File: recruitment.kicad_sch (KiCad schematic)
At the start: 14 parts, among them SW1 SW_SPST

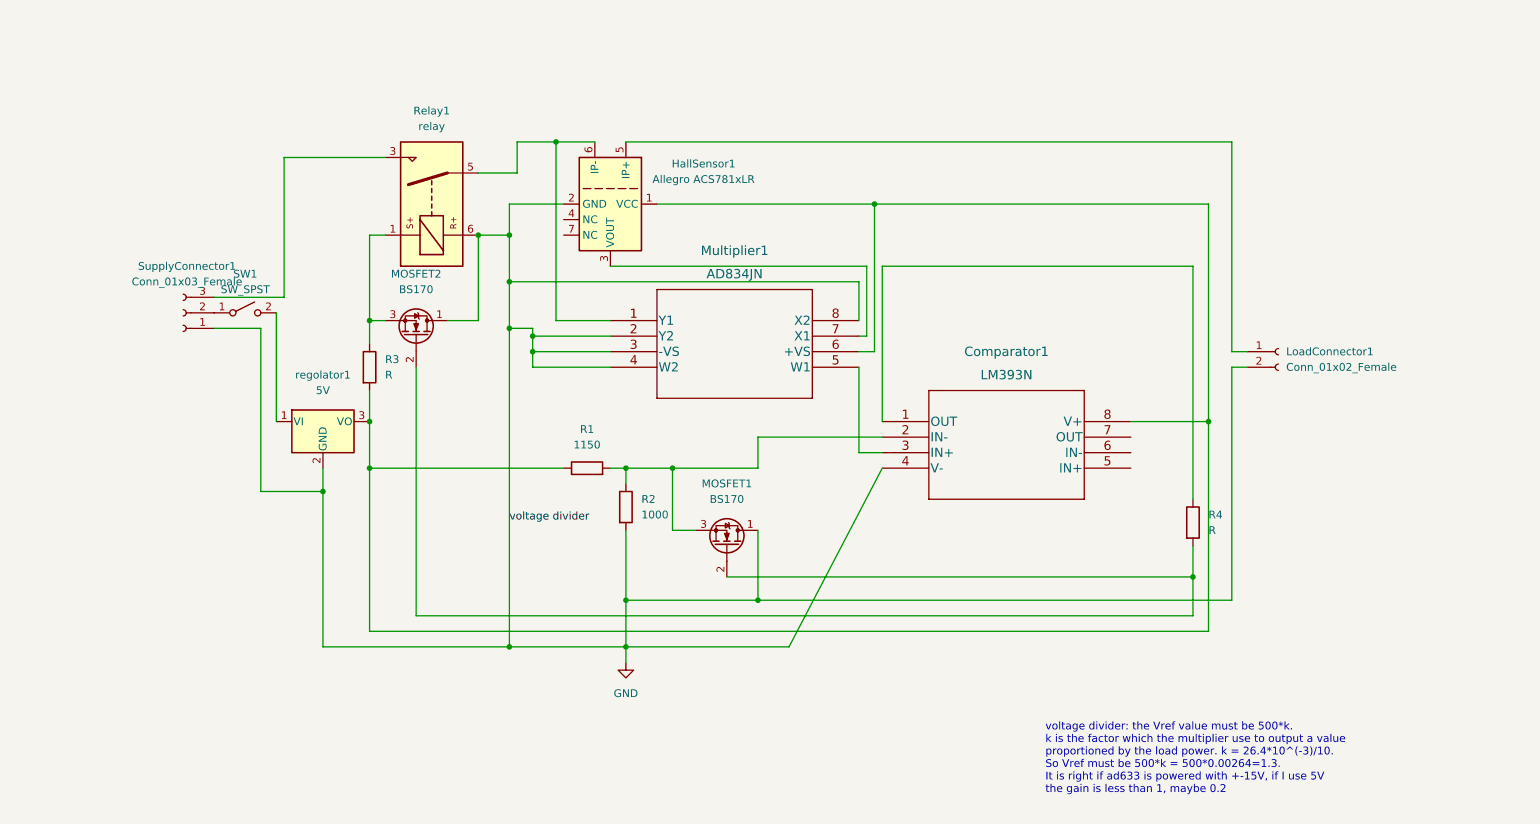
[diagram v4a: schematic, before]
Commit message: TODO: mosfet depletion channel p
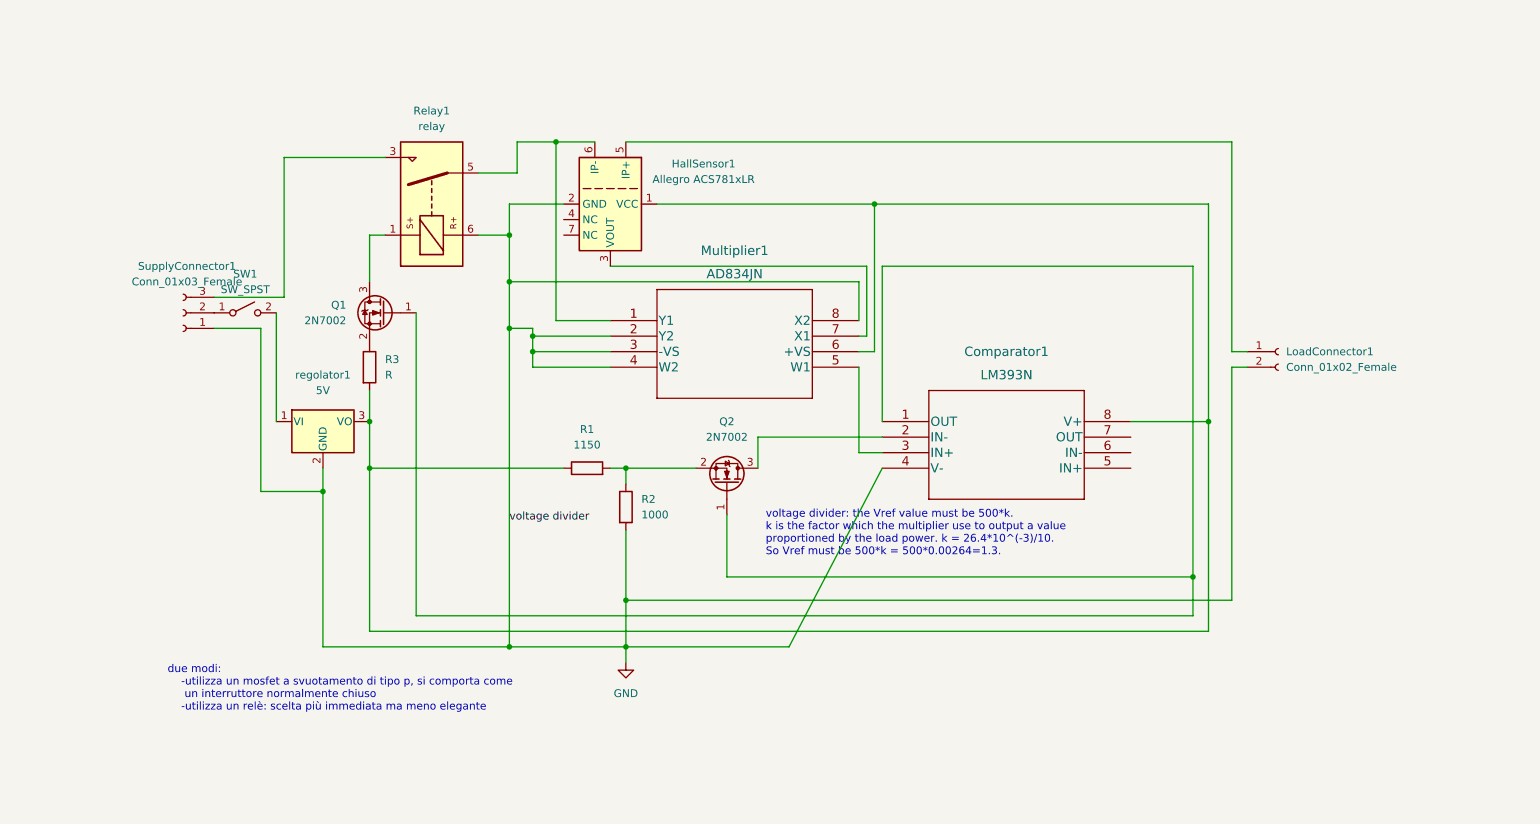
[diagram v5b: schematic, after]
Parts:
- removed MOSFET1, MOSFET2: BS170, Package_TO_SOT_THT:TO-92_Inline, symbol Transistor_FET:BS170
- removed R4: R, Resistor_SMD:R_2816_7142Metric, symbol Device:R
- added Q1, Q2: 2N7002, Package_TO_SOT_SMD:SOT-23, symbol Transistor_FET:2N7002
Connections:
- net at R1.2, R2.1: now also Q2.2 (S); no longer Comparator1.2 (IN-)
- net at R3.1: now also Q1.2 (S); no longer Relay1.1
- net at Comparator1.1 (OUT): now also Q1.1 (G), Q2.1 (G)
- new net: Comparator1.2 (IN-), Q2.3 (D)
- new net: Q1.3 (D), Relay1.1
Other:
- note added: "due modi: -utilizza un mosfet a svuotamento di tipo p, si comporta come un interruttore normalmente chiuso -utilizza un relè: scelta più immediata ma meno elegante"
- note added: "voltage divider: the Vref value must be 500*k. k is the factor which the multiplier use to output a value proportioned by the load power. k = 26.4*10^(-3)/10. So Vref must be 500*k = 500*0.00264=1.3."
- note removed: "voltage divider: the Vref value must be 500*k. k is the factor which the multiplier use to output a value proportioned by the load power. k = 26.4*10^(-3)/10. So Vref must be 500*k = 500*0.00264=1.3. It is right if ad633 is powered with +-15V, if I use 5V the gain is less than 1, maybe 0.2"

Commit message: remove casino, TODO: add flipflp sr, check AD834jn
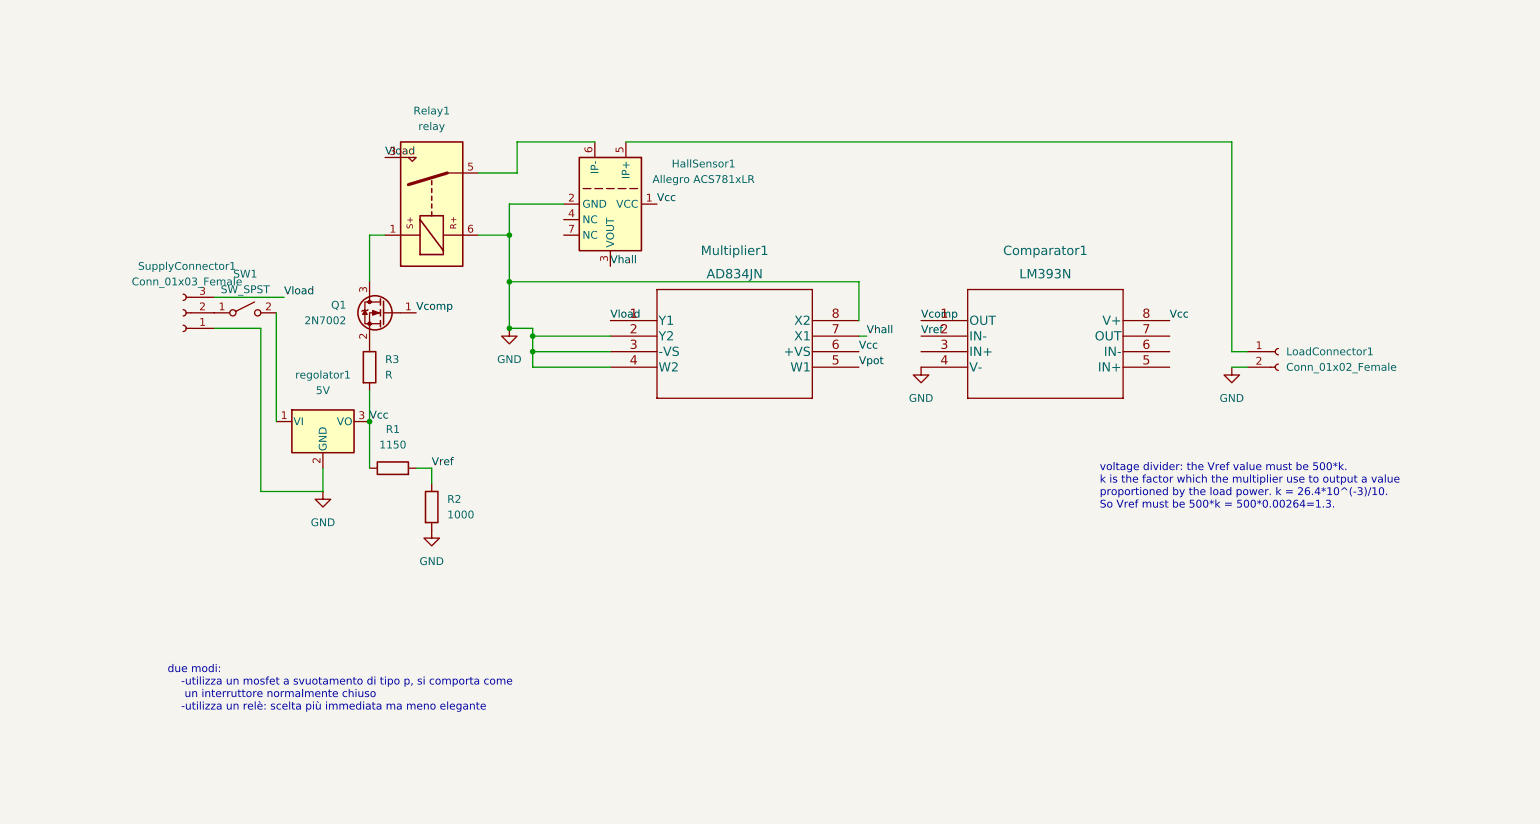
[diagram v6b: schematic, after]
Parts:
- removed Q2: 2N7002, Package_TO_SOT_SMD:SOT-23, symbol Transistor_FET:2N7002
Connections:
- net Vref: now reaches R1.2, R2.1
- net Vref: now also Comparator1.2 (IN-)
- net Vcc: now reaches Comparator1.8 (V+), HallSensor1.1 (VCC), Multiplier1.6 (+VS), R1.1, R3.2, regolator1.3 (VO)
- net Vhall: now reaches HallSensor1.3 (VOUT), Multiplier1.7 (X1)
- net at HallSensor1.6 (IP-), Relay1.5: no longer Multiplier1.1 (Y1)
- net Vcomp: now reaches Comparator1.1 (OUT), Q1.1 (G)
- net at Comparator1.3 (IN+): no longer Multiplier1.5 (W1)
- net Vload: now reaches Relay1.3, SupplyConnector1.3 (Pin_3)
- net Vload: now also Multiplier1.1 (Y1)
- new net Vpot: Multiplier1.5 (W1)
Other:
- moved on the sheet: Comparator1, R1, R2

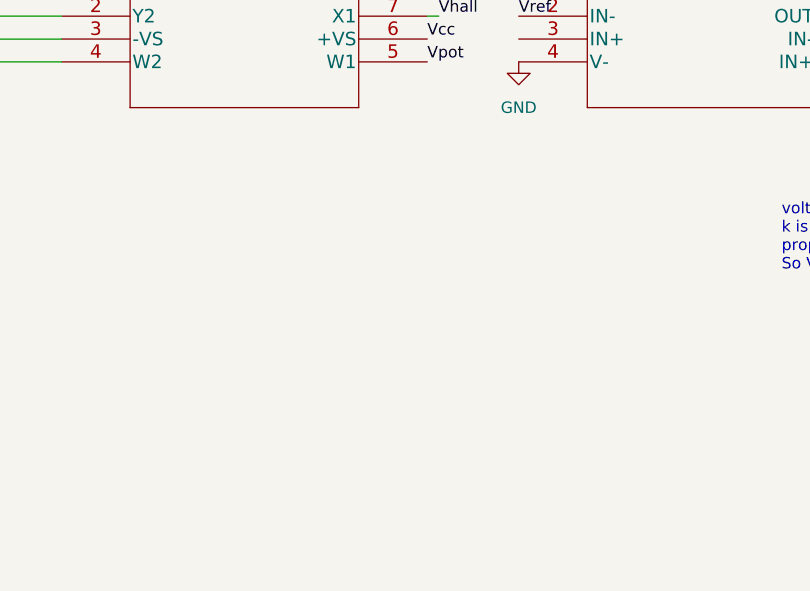
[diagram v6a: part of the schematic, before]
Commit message: added flipflop, TODO: connect Vff to MOSFET relay
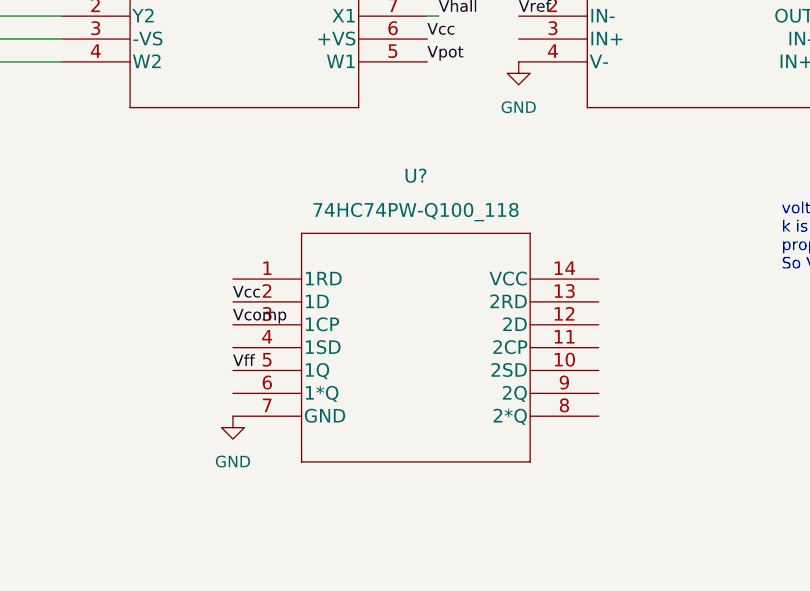
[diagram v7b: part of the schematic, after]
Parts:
- added U?: 74HC74PW-Q100_118, TSSOP14_SOT402-1_NEX, symbol 2023-03-15_18-44-27:74HC74PW-Q100_118
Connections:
- net GND: now also U?.7 (GND)
- net Vcc: now also U?.2 (1D)
- net Vcomp: now also U?.3 (1CP)
- new net Vff: U?.5 (1Q)

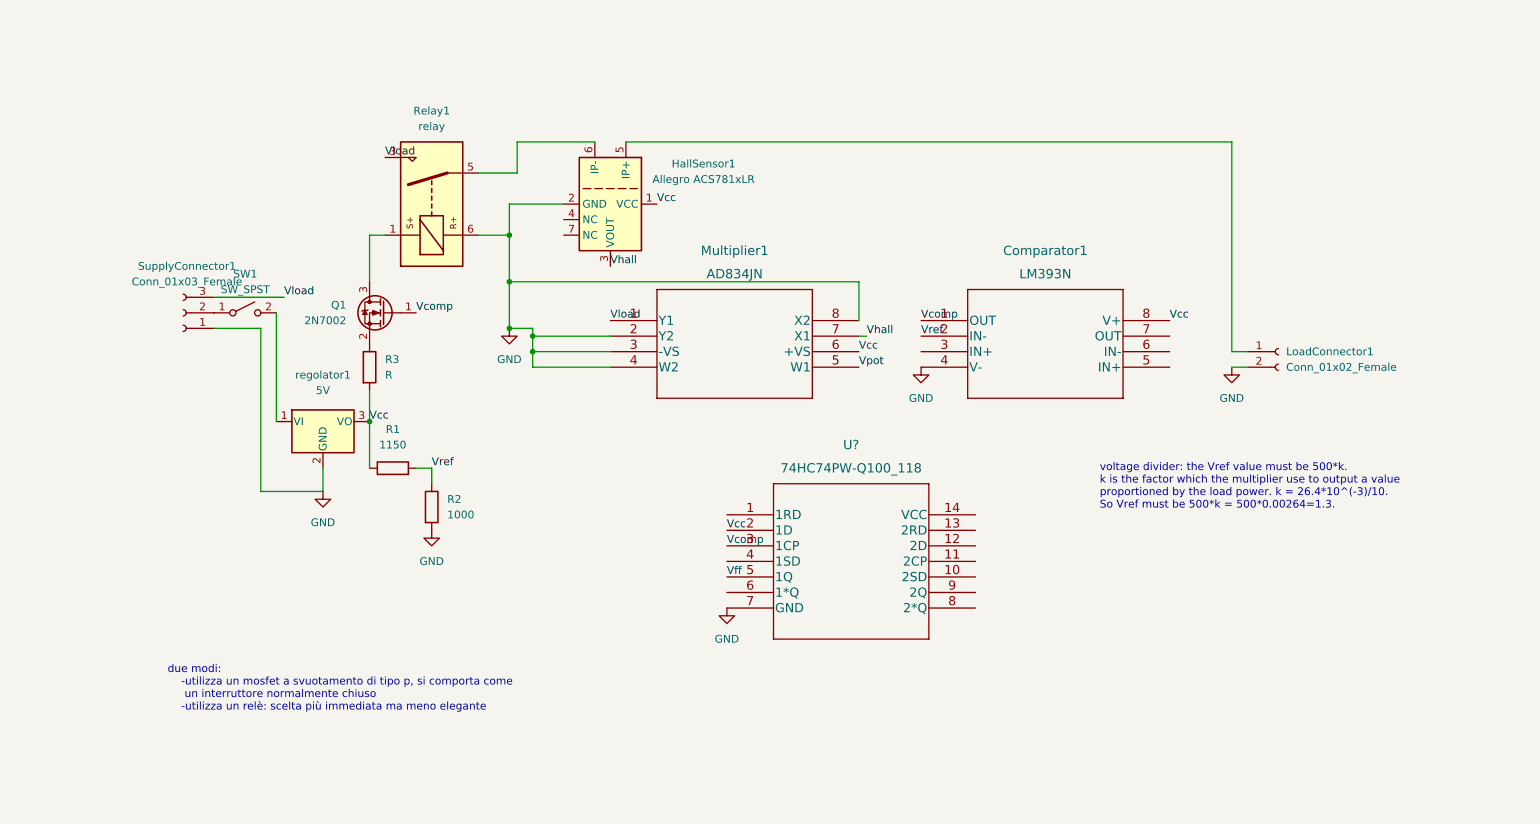
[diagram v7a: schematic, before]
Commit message: add AD835, correct voltages and wires
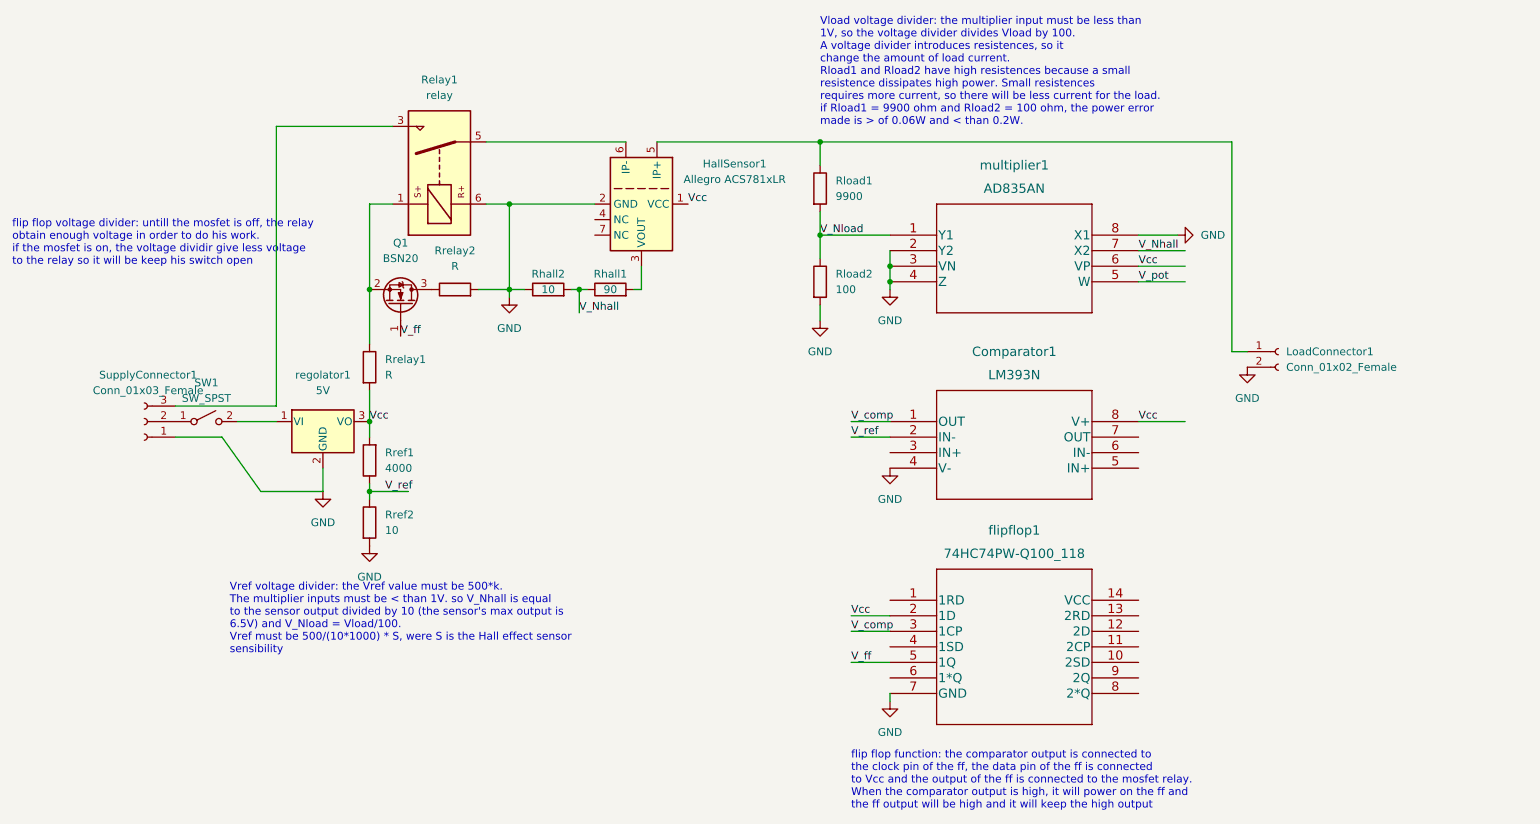
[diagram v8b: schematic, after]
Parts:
- removed Multiplier1: AD834JN, LM393:LM393N, symbol 2023-03-13_17-57-03:AD834JN
- removed Q1: 2N7002, Package_TO_SOT_SMD:SOT-23, symbol Transistor_FET:2N7002
- added Q1: BSN20, Package_TO_SOT_SMD:SOT-23, symbol Transistor_FET:BSN20
- added Rhall1: 90, symbol Device:R
- added Rhall2: 10, symbol Device:R
- added Rload1: 9900, symbol Device:R
- added Rload2: 100, symbol Device:R
- added Rrelay2: R, symbol Device:R
- added multiplier1: AD835AN, N_8_ADI, symbol 2023-03-17_09-04-10:AD835AN
- Rref1: renamed from R1; value 1150 -> 4000
- Rref2: renamed from R2; value 1000 -> 10
- gave numbers to parts that had none: 1
- renumbered R3 to Rrelay1
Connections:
- net GND: now also Rhall2.1, Rload2.2, Rrelay2.2, multiplier1.2 (Y2), multiplier1.3 (VN), multiplier1.4 (Z), multiplier1.8 (X1)
- net Vcc: now also Rref1.2, multiplier1.6 (VP); no longer Rref1.1
- net at Rrelay1.1: now also Relay1.1, Q1.2 (S)
- net at HallSensor1.5 (IP+), LoadConnector1.1 (Pin_1): now also Rload1.1
- net Vcomp renamed V_comp
- net Vff renamed V_ff
- net V_ff: now also Q1.1 (G)
- net Vhall: no longer names the net of HallSensor1.3 (VOUT)
- net Vhall: now also Rhall1.2
- net Vload: no longer names the net of Relay1.3, SupplyConnector1.3 (Pin_3)
- net Vref renamed V_ref
- net V_ref: now also Rref1.1; no longer Rref1.2
- new net: Q1.3 (D), Rrelay2.1
- new net V_Nhall: Rhall1.1, Rhall2.2, multiplier1.7 (X2)
- new net V_Nload: Rload1.2, Rload2.1, multiplier1.1 (Y1)
- new net V_pot: multiplier1.5 (W)
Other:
- note added: "Vload voltage divider: the multiplier input must be less than 1V, so the voltage divider divides Vload by 100. A voltage divider introduces resistences, so it change the amount of load current. Rload1 and Rload2 have high resistences because a small resistence dissipates high power. Small resistences requires more current, so there will be less current for the load. if Rload1 = 9900 ohm and Rload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"
- note added: "Vref voltage divider: the Vref value must be 500*k. The multiplier inputs must be < than 1V. so V_Nhall is equal to the sensor output divided by 10 (the sensor's max output is 6.5V) and V_Nload = Vload/100. Vref must be 500/(10*1000) * S, were S is the Hall effect sensor sensibility"
- note added: "flip flop function: the comparator output is connected to the clock pin of the ff, the data pin of the ff is connected to Vcc and the output of the ff is connected to the mosfet relay. When the comparator output is high, it will power on the ff and the ff output will be high and it will keep the high output"
- note added: "flip flop voltage divider: untill the mosfet is off, the relay obtain enough voltage in order to do his work. if the mosfet is on, the voltage dividir give less voltage to the relay so it will be keep his switch open"
- note removed: "due modi: -utilizza un mosfet a svuotamento di tipo p, si comporta come un interruttore normalmente chiuso -utilizza un relè: scelta più immediata ma meno elegante"
- note removed: "voltage divider: the Vref value must be 500*k. k is the factor which the multiplier use to output a value proportioned by the load power. k = 26.4*10^(-3)/10. So Vref must be 500*k = 500*0.00264=1.3."
- moved on the sheet: Comparator1, HallSensor1, Relay1, Rref1, Rref2, SW1, SupplyConnector1, flipflop1
